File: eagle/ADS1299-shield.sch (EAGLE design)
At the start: 118 parts, among them IC1 24AA256UID, IC2 TPS72325DBVT, IC3 TPS73225DBVT, J8 Electrode Connector, U1 ADS1299IPAG, U2 TXB0108PWR, U3 TXB0108PWR

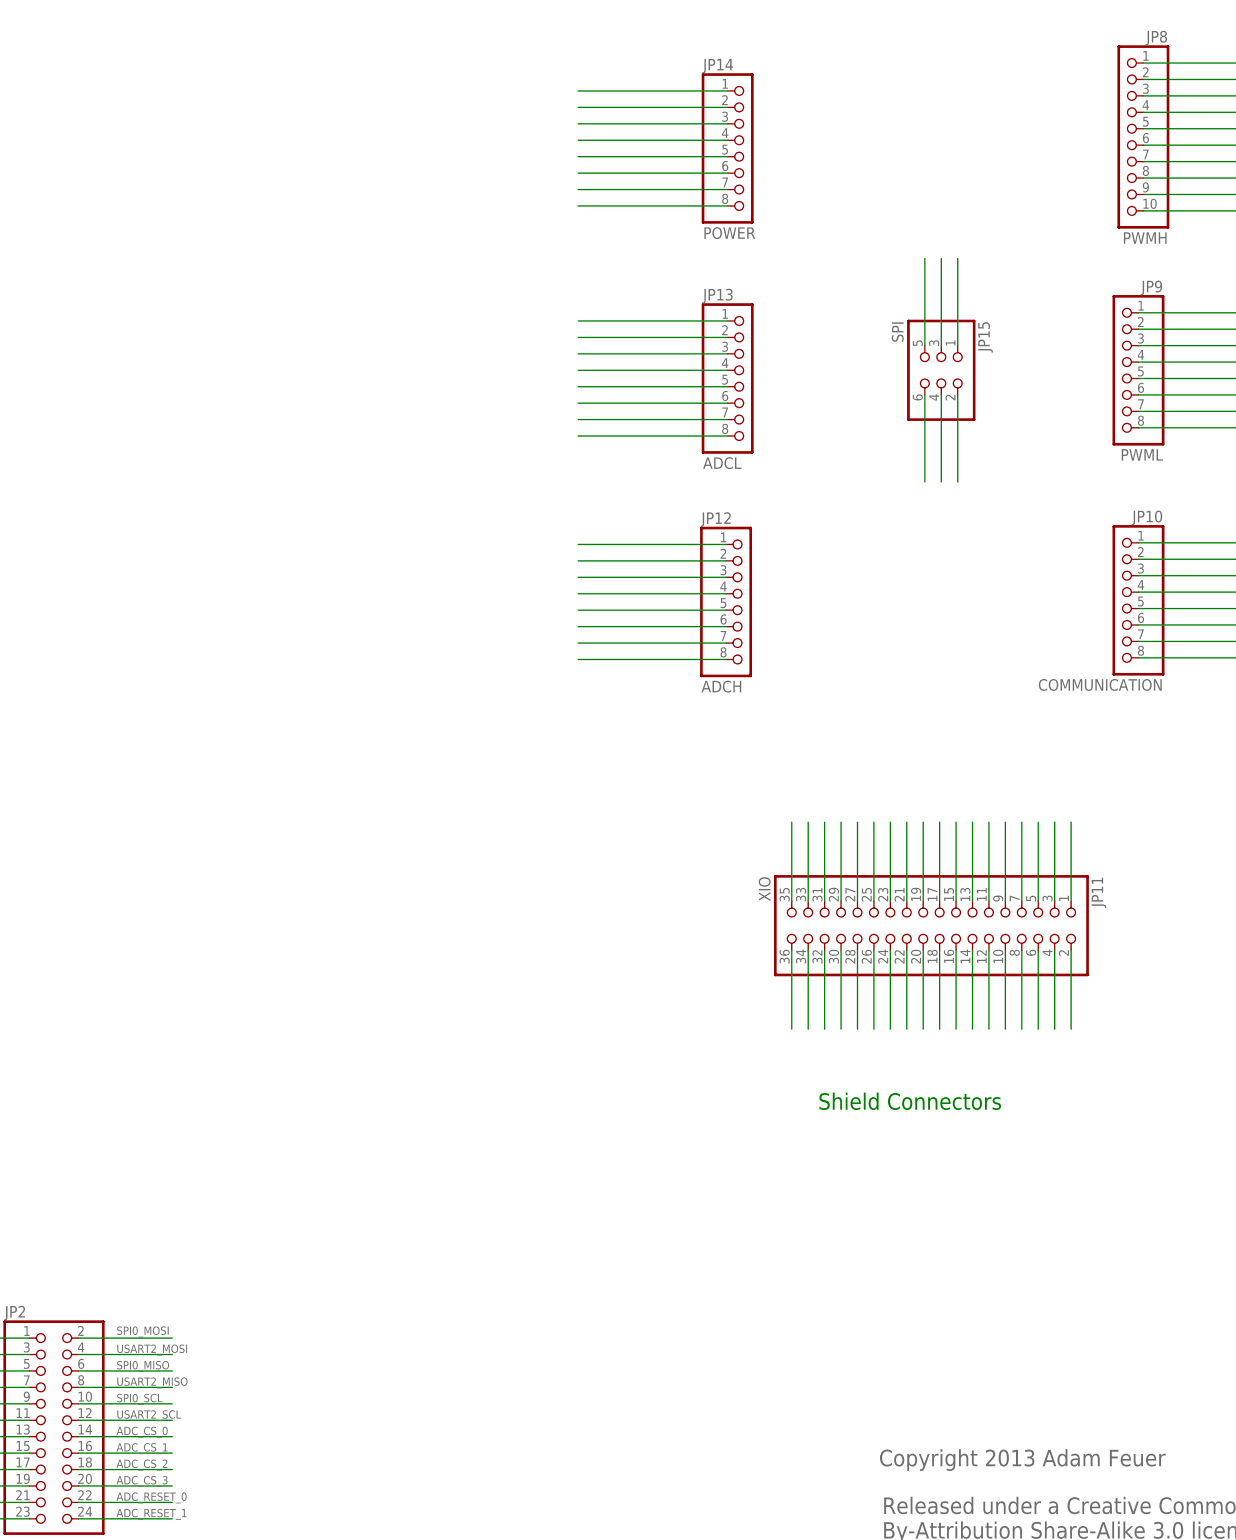
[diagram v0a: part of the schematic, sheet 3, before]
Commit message: wires and labels added for SPI and XIO connectors
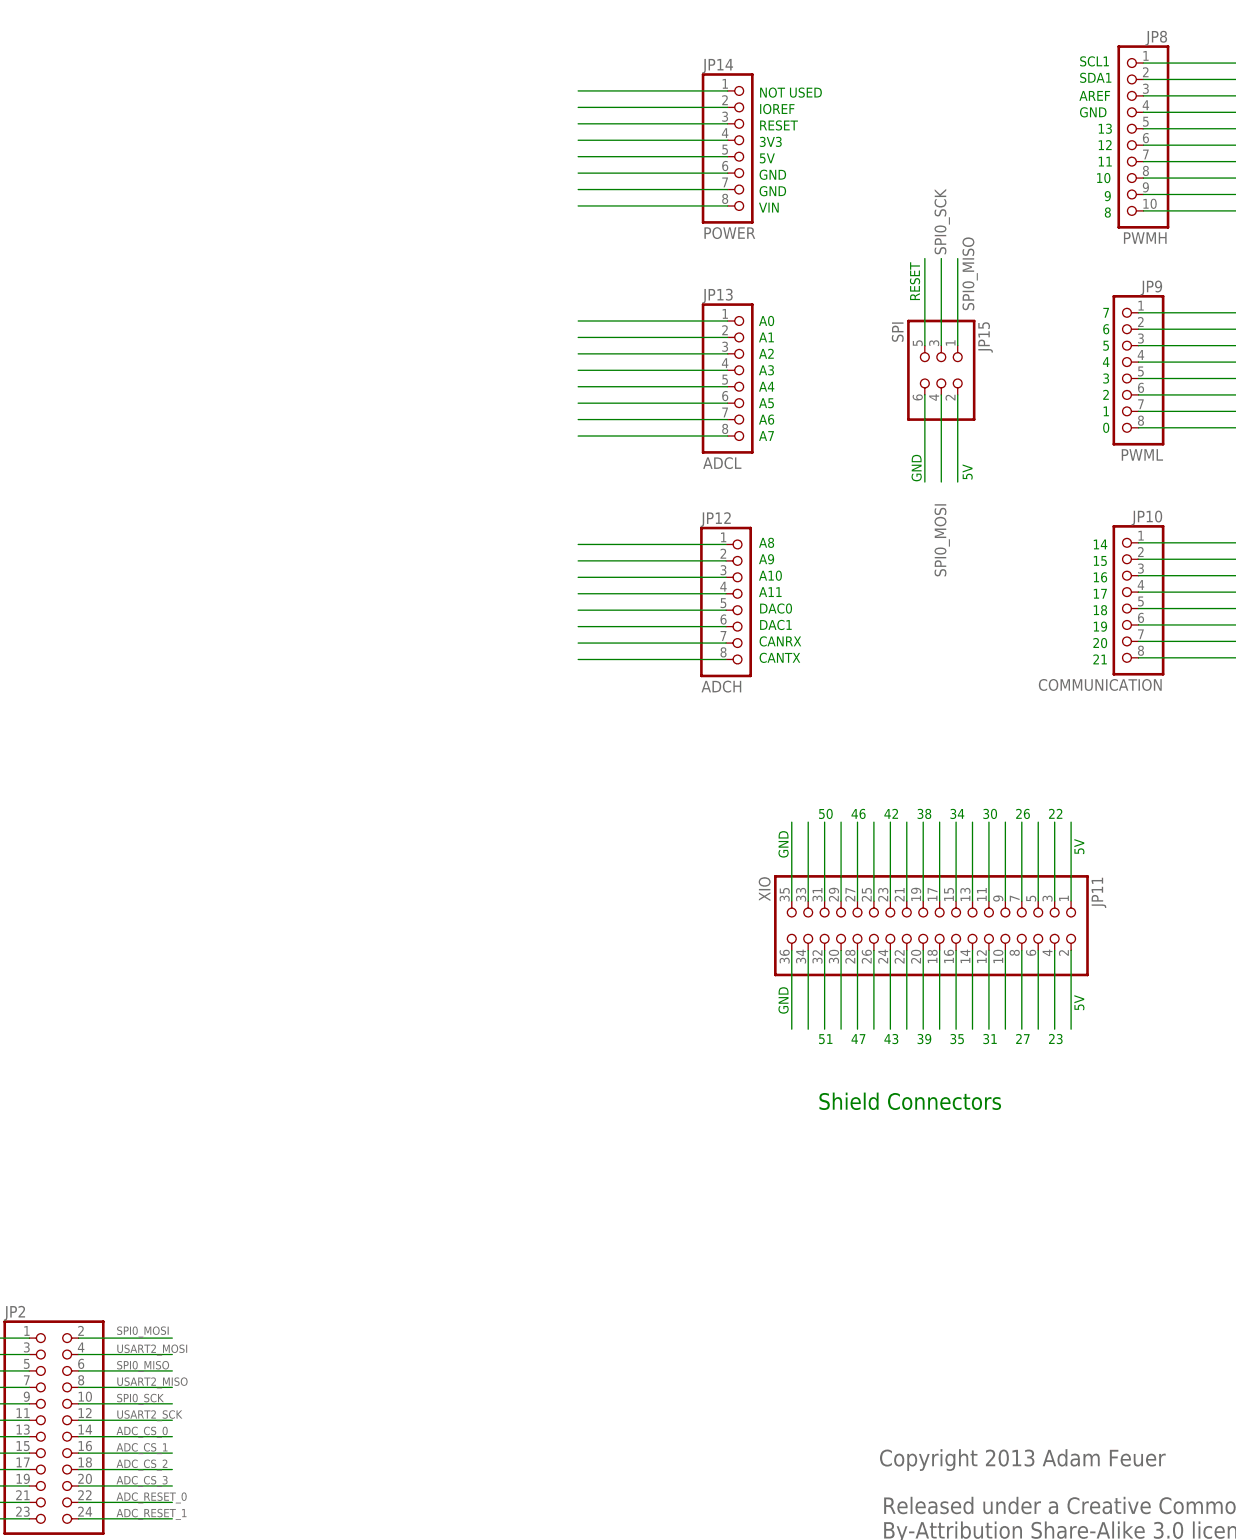
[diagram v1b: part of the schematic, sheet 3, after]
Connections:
- net N$70 renamed 5V
- net N$71 renamed RESET
- net USART2_SCL renamed USART2_SCK
- removed net N$69: JP15.1
- removed net N$72: JP15.3
- removed net N$73: JP15.6
- removed net N$74: JP15.4
- removed net SPI0_SCL: JP2.10
- new net SPI0_SCK: JP15.3, JP2.10
- net GND: now also JP15.6
- net SPI0_MISO: now also JP15.1
- net SPI0_MOSI: now also JP15.4
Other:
- note added: "0"
- note added: "1"
- note added: "10"
- note added: "11"
- note added: "12"
- note added: "13"
- note added: "14"
- note added: "15"
- note added: "16"
- note added: "17"
- note added: "18"
- note added: "19"
- note added: "2"
- note added: "20"
- note added: "21"
- note added: "22"
- note added: "23"
- note added: "26"
- note added: "27"
- note added: "3"
- note added: "30"
- note added: "31"
- note added: "34"
- note added: "35"
- note added: "38"
- note added: "39"
- note added: "3V3"
- note added: "4"
- note added: "42"
- note added: "43"
- note added: "46"
- note added: "47"
- note added: "5"
- note added: "50"
- note added: "51"
- note added: "5V"
- note added: "6"
- note added: "7"
- note added: "8"
- note added: "9"
- note added: "A0"
- note added: "A1"
- note added: "A10"
- note added: "A11"
- note added: "A2"
- note added: "A3"
- note added: "A4"
- note added: "A5"
- note added: "A6"
- note added: "A7"
- note added: "A8"
- note added: "A9"
- note added: "AREF"
- note added: "CANRX"
- note added: "CANTX"
- note added: "DAC0"
- note added: "DAC1"
- note added: "GND"
- note added: "IOREF"
- note added: "NOT USED"
- note added: "RESET"
- note added: "SCL1"
- note added: "SDA1"
- note added: "VIN"
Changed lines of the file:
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@@
 <text x="325.628" y="37.592" size="2.54" layer="95">Copyright 2013 Adam Feuer</text>
 <text x="316.23" y="92.71" size="2.54" layer="91">Shield Connectors</text>
+<text x="356.616" y="254" size="1.524" layer="91">SCL1</text>
+<text x="356.616" y="251.46" size="1.524" layer="91">SDA1</text>
+<text x="356.616" y="248.666" size="1.524" layer="91">AREF</text>
+<text x="356.616" y="246.126" size="1.524" layer="91">GND</text>
+<text x="359.41" y="243.586" size="1.524" layer="91">13</text>
+<text x="359.41" y="241.046" size="1.524" layer="91">12</text>
+<text x="359.41" y="238.506" size="1.524" layer="91">11</text>
+<text x="359.156" y="235.966" size="1.524" layer="91">10</text>
+<text x="360.426" y="233.172" size="1.524" layer="91">9</text>
+<text x="360.426" y="230.632" size="1.524" layer="91">8</text>
+<text x="358.648" y="179.324" size="1.524" layer="91">14</text>
+<text x="358.648" y="176.784" size="1.524" layer="91">15</text>
+<text x="358.648" y="174.244" size="1.524" layer="91">16</text>
+<text x="358.648" y="171.704" size="1.524" layer="91">17</text>
+<text x="358.648" y="169.164" size="1.524" layer="91">18</text>
+<text x="358.648" y="166.624" size="1.524" layer="91">19</text>
+<text x="358.648" y="164.084" size="1.524" layer="91">20</text>
+<text x="358.648" y="161.544" size="1.524" layer="91">21</text>
+<text x="360.172" y="215.138" size="1.524" layer="91">7</text>
+<text x="360.172" y="212.598" size="1.524" layer="91">6</text>
+<text x="360.172" y="210.058" size="1.524" layer="91">5</text>
+<text x="360.172" y="207.518" size="1.524" layer="91">4</text>
+<text x="360.172" y="204.978" size="1.524" layer="91">3</text>
+<text x="360.172" y="202.438" size="1.524" layer="91">2</text>
+<text x="360.172" y="199.898" size="1.524" layer="91">1</text>
+<text x="360.172" y="197.358" size="1.524" layer="91">0</text>
+<text x="307.086" y="179.578" size="1.524" layer="91">A8</text>
+<text x="307.086" y="177.038" size="1.524" layer="91">A9</text>
+<text x="307.086" y="174.498" size="1.524" layer="91">A10</text>
+<text x="307.086" y="171.958" size="1.524" layer="91">A11</text>
+<text x="307.086" y="169.418" size="1.524" layer="91">DAC0</text>
+<text x="307.086" y="166.878" size="1.524" layer="91">DAC1</text>
+<text x="307.086" y="164.338" size="1.524" layer="91">CANRX</text>
+<text x="307.086" y="161.798" size="1.524" layer="91">CANTX</text>
+<text x="307.086" y="213.868" size="1.524" layer="91">A0</text>
+<text x="307.086" y="211.328" size="1.524" layer="91">A1</text>
+<text x="307.086" y="208.788" size="1.524" layer="91">A2</text>
+<text x="307.086" y="206.248" size="1.524" layer="91">A3</text>
+<text x="307.086" y="203.708" size="1.524" layer="91">A4</text>
+<text x="307.086" y="201.168" size="1.524" layer="91">A5</text>
+<text x="307.086" y="198.628" size="1.524" layer="91">A6</text>
+<text x="307.086" y="196.088" size="1.524" layer="91">A7</text>
+<text x="307.086" y="249.174" size="1.524" layer="91">NOT USED</text>
+<text x="307.086" y="246.634" size="1.524" layer="91">IOREF</text>
+<text x="307.086" y="244.094" size="1.524" layer="91">RESET</text>
+<text x="307.086" y="241.554" size="1.524" layer="91">3V3</text>
+<text x="307.086" y="239.014" size="1.524" layer="91">5V</text>
+<text x="307.086" y="236.474" size="1.524" layer="91">GND</text>
+<text x="307.086" y="233.934" size="1.524" layer="91">GND</text>
+<text x="307.086" y="231.394" size="1.524" layer="91">VIN</text>
+<text x="340.106" y="189.992" size="1.524" layer="91" rot="R90">5V</text>
+<text x="332.232" y="189.738" size="1.524" layer="91" rot="R90">GND</text>
+<text x="331.978" y="217.678" size="1.524" layer="91" rot="R90">RESET</text>
+<text x="357.378" y="132.08" size="1.524" layer="91" rot="R90">5V</text>
+<text x="357.378" y="107.95" size="1.524" layer="91" rot="R90">5V</text>
+<text x="311.658" y="107.442" size="1.524" layer="91" rot="R90">GND</text>
+<text x="311.658" y="131.572" size="1.524" layer="91" rot="R90">GND</text>
+<text x="351.79" y="137.668" size="1.524" layer="91">22</text>
+<text x="351.79" y="102.87" size="1.524" layer="91">23</text>
+<text x="346.71" y="137.668" size="1.524" layer="91">26</text>
+<text x="341.63" y="137.668" size="1.524" layer="91">30</text>
+<text x="336.55" y="137.668" size="1.524" layer="91">34</text>
+<text x="331.47" y="137.668" size="1.524" layer="91">38</text>
+<text x="326.39" y="137.668" size="1.524" layer="91">42</text>
+<text x="321.31" y="137.668" size="1.524" layer="91">46</text>
+<text x="316.23" y="137.668" size="1.524" layer="91">50</text>
+<text x="346.71" y="102.87" size="1.524" layer="91">27</text>
+<text x="341.63" y="102.87" size="1.524" layer="91">31</text>
+<text x="336.55" y="102.87" size="1.524" layer="91">35</text>
+<text x="331.47" y="102.87" size="1.524" layer="91">39</text>
+<text x="326.39" y="102.87" size="1.524" layer="91">43</text>
+<text x="321.31" y="102.87" size="1.524" layer="91">47</text>
+<text x="316.23" y="102.87" size="1.524" layer="91">51</text>
 </plain>
 <instances>
@@
 <label x="207.772" y="57.912" size="1.27" layer="95"/>
 </segment>
+<segment>
+<pinref part="JP15" gate="A" pin="4"/>
+<wire x1="335.28" y1="203.2" x2="335.28" y2="189.738" width="0.1524" layer="91"/>
+<label x="336.042" y="175.006" size="1.778" layer="95" rot="R90"/>
+</segment>
 </net>
 <net name="USART2_MOSI" class="0">
@@
 <label x="207.772" y="52.578" size="1.27" layer="95"/>
 </segment>
+<segment>
+<pinref part="JP15" gate="A" pin="1"/>
+<wire x1="337.82" y1="210.82" x2="337.82" y2="224.282" width="0.1524" layer="91"/>
+<label x="340.36" y="216.154" size="1.778" layer="95" rot="R90"/>
+</segment>
 </net>
 <net name="ADC_CS_3" class="0">
@@
 </segment>
 </net>
-<net name="USART2_SCL" class="0">
+<net name="USART2_SCK" class="0">
 <segment>
 <pinref part="JP2" gate="A" pin="12"/>
 <wire x1="201.93" y1="44.704" x2="216.408" y2="44.704" width="0.1524" layer="91"/>
 <label x="207.772" y="44.958" size="1.27" layer="95"/>
-</segment>
-</net>
-<net name="SPI0_SCL" class="0">
-<segment>
-<pinref part="JP2" gate="A" pin="10"/>
-<wire x1="201.93" y1="47.244" x2="216.408" y2="47.244" width="0.1524" layer="91"/>
-<label x="207.772" y="47.498" size="1.27" layer="95"/>
 </segment>
 </net>
@@
 </segment>
 </net>
-<net name="N$69" class="0">
-<segment>
-<pinref part="JP15" gate="A" pin="1"/>
-<wire x1="337.82" y1="210.82" x2="337.82" y2="224.282" width="0.1524" layer="91"/>
-</segment>
-</net>
-<net name="N$70" class="0">
+<net name="5V" class="0">
 <segment>
 <pinref part="JP15" gate="A" pin="2"/>
@@
 </segment>
 </net>
-<net name="N$71" class="0">
+<net name="RESET" class="0">
 <segment>
 <pinref part="JP15" gate="A" pin="5"/>
@@
 </segment>
 </net>
-<net name="N$72" class="0">
+<net name="SPI0_SCK" class="0">
 <segment>
 <pinref part="JP15" gate="A" pin="3"/>
 <wire x1="335.28" y1="210.82" x2="335.28" y2="224.282" width="0.1524" layer="91"/>
-</segment>
-</net>
-<net name="N$73" class="0">
+<label x="336.042" y="224.79" size="1.778" layer="95" rot="R90"/>
+</segment>
+<segment>
+<pinref part="JP2" gate="A" pin="10"/>
+<wire x1="201.93" y1="47.244" x2="216.408" y2="47.244" width="0.1524" layer="91"/>
+<label x="207.772" y="47.498" size="1.27" layer="95"/>
+</segment>
+</net>
+<net name="GND" class="0">
 <segment>
 <pinref part="JP15" gate="A" pin="6"/>
@@
 </segment>
 </net>
-<net name="N$74" class="0">
-<segment>
-<pinref part="JP15" gate="A" pin="4"/>
-<wire x1="335.28" y1="203.2" x2="335.28" y2="189.738" width="0.1524" layer="91"/>
-</segment>
-</net>
